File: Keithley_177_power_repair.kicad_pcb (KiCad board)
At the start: 2 copper layers, 58 x 46 mm, 7 parts, among them T1 RAC20-DK, T101 Transformer, U1 R-78E5.0-1.0

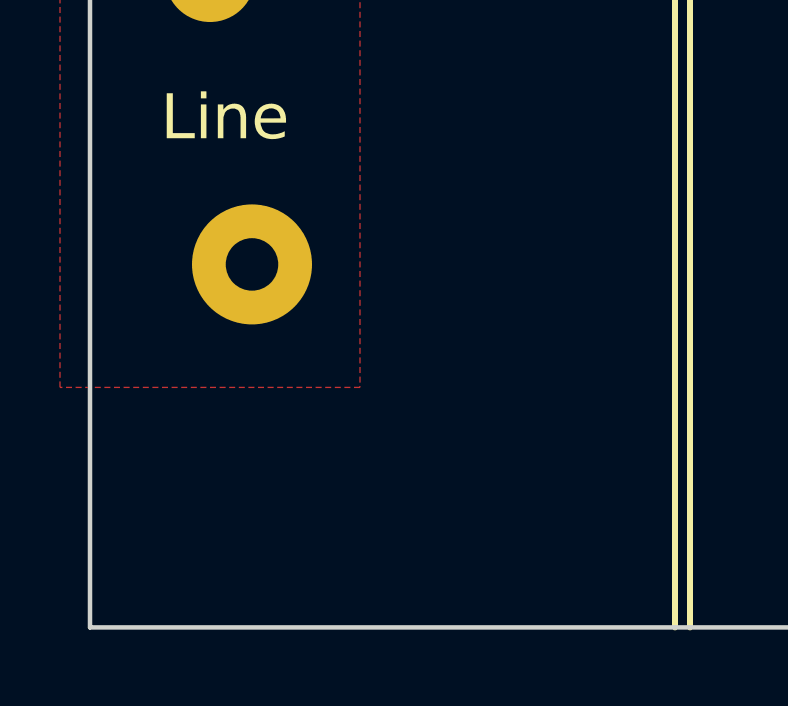
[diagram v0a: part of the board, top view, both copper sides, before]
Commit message: Update Keithley_177_power_repair.kicad_pcb
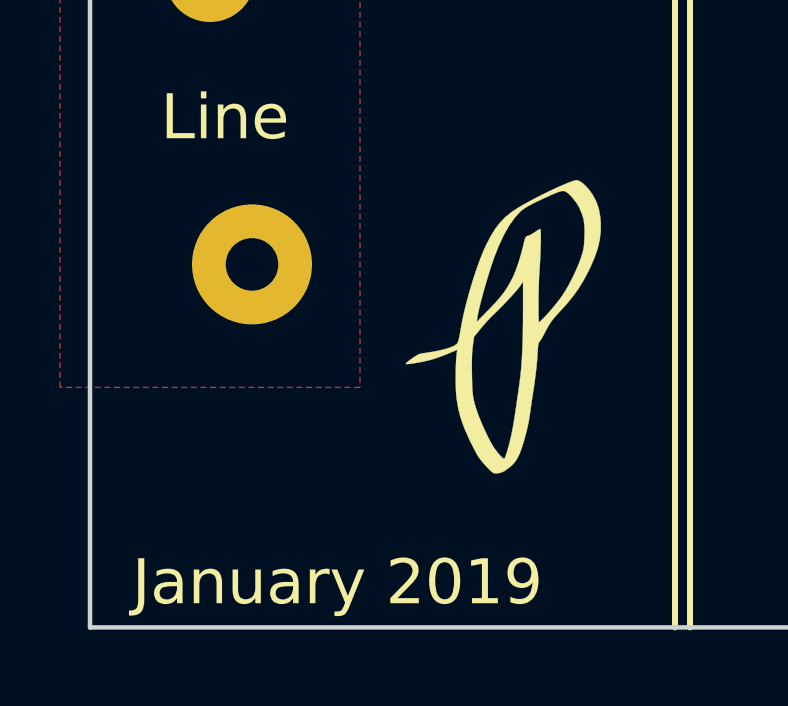
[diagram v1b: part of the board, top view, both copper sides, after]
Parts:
- added G***: LOGO, PL_logo:logo_height_10mm, F.Cu at (43.8, 80.0)
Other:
- board text added: "January 2019"
- board text added: "Keithly 177 Transformer Replacment"
